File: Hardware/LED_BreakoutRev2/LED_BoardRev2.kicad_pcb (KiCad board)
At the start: 2 copper layers, 33 parts, among them Q1 BSS214NW, Q2 BSS214NW, Q3 BSS214NW, Q4 BSS214NW, Q5 BSS214NW, Q6 BSS214NW

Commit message: Concept LED layout
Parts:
- removed R13, R14: 4, MRDT_Devices:Stupid 4 Ohm Resistor
- Conn1, Q1, Q2, Q3, Q4, Q5, Q6, R2, R3: moved to B.Cu
- R1: value 250 -> 325; moved to B.Cu
- R10: value 4 -> 16; footprint MRDT_Devices:Stupid 4 Ohm Resistor -> Resistor_SMD:R_2512_6332Metric_Pad1.40x3.35mm_HandSolder; moved to B.Cu
- R11: value 4 -> 237; footprint MRDT_Devices:Stupid 4 Ohm Resistor -> Resistor_SMD:R_2512_6332Metric_Pad1.40x3.35mm_HandSolder; moved to B.Cu
- R12: value 235 -> 16; moved to B.Cu
- R4, R6, R8: value 150 -> 325; moved to B.Cu
- R5, R7: value 41 -> 39; moved to B.Cu
- R9: value 235 -> 237; moved to B.Cu
- moved Q4 167.2 mm to (55.8, 25.0), turned to 180 degrees
- moved Q2 146.0 mm to (53.5, 37.5), turned to 180 degrees
- moved Q3 139.5 mm to (71.4, 44.3), turned to 180 degrees
- moved R5 138.7 mm to (81.0, 22.1), turned to 180 degrees
- moved R4 133.2 mm to (81.0, 27.0), turned to 180 degrees
- moved R8 124.5 mm to (90.0, 22.1), turned to 180 degrees
- moved R3 121.5 mm to (102.5, 34.7), turned to 180 degrees
- moved R10 121.0 mm to (90.0, 27.0), turned to 180 degrees
- moved Q5 118.6 mm to (83.1, 41.0), turned to 180 degrees
- moved R2 115.8 mm to (102.5, 29.8), turned to 180 degrees
- moved R6 110.0 mm to (102.5, 39.6), turned to 180 degrees
- moved R11 109.9 mm to (93.4, 31.9), turned to 180 degrees
- moved R7 106.9 mm to (111.5, 34.7), turned to 180 degrees
- moved R1 106.5 mm to (111.5, 29.8), turned to 180 degrees
- moved Q6 101.4 mm to (109.4, 48.8), turned to 180 degrees
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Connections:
- R10 pad 2: Net-(R10-Pad2) -> Net-(Q5-Pad3)
- R11 pad 1: Net-(R10-Pad2) -> Net-(D11-Pad1)
- R11 pad 2: Net-(Q5-Pad3) -> Net-(Q4-Pad3)
- R12 pad 1: Net-(D11-Pad1) -> Net-(D12-Pad1)
- R12 pad 2: Net-(Q4-Pad3) -> Net-(Q5-Pad3)
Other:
- board outline added: 53.9 x 53.9 mm

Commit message: Still moving footprints
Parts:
- D5, D7: footprint MRDT_Devices:275nm LED -> Footprints:SU CULCN1.VC
- moved D7 12.3 mm to (184.7, 82.0), turned to 90 degrees
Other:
- outline, holes or cut-outs redrawn
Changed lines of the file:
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@@
   (net 23 "Net-(D9-Pad1)")
   (net 24 "Net-(D11-Pad1)")
-  (footprint "MRDT_Devices:275nm LED" (layer "F.Cu")
+  (footprint "Footprints:SU CULCN1.VC" (layer "F.Cu")
     (at 166.4016 112.3104)
     (property "Sheetfile" "LED_BoardRev2.kicad_sch")
     (property "Sheetname" "")
     (attr smd)
-    (fp_text reference "D5" (at 0.33 -2.57 unlocked) (layer "F.SilkS")
-      (effects (font (size 1 1) (thickness 0.15)))
-    )
-    (fp_text value "275nm" (at 0.33 2.91 unlocked) (layer "F.Fab")
-      (effects (font (size 1 1) (thickness 0.15)))
-    )
-    (fp_text user "${REFERENCE}" (at 0.33 4.41 unlocked) (layer "F.Fab")
-      (effects (font (size 1 1) (thickness 0.15)))
-    )
-    (fp_rect (start -1.68 1.86) (end 1.82 -1.64) (layer "F.SilkS") (width 0.12) (fill none))
-    (pad "+" smd roundrect (at 1.435 0.10775) (size 0.57 3.3155) (layers "F.Cu" "F.Paste" "F.Mask") (roundrect_rratio 0.1))
-    (pad "-" smd roundrect (at -1.295 0.11) (size 0.57 3.32) (layers "F.Cu" "F.Paste" "F.Mask") (roundrect_rratio 0.1))
-    (pad "ESD" smd roundrect (at 0.07 0.11) (size 1.32 3.32) (layers "F.Cu" "F.Paste" "F.Mask") (roundrect_rratio 0.1))
+    (fp_text reference "D5" (at 0 -4 unlocked) (layer "F.SilkS")
+      (effects (font (size 1 1) (thickness 0.15)))
+    )
+    (fp_text value "275nm" (at 0 4.1 unlocked) (layer "F.Fab")
+      (effects (font (size 1 1) (thickness 0.15)))
+    )
+    (fp_text user "${REFERENCE}" (at 0 6 unlocked) (layer "F.Fab")
+      (effects (font (size 1 1) (thickness 0.15)))
+    )
+    (fp_line (start -2.8 -3.1) (end 2.8 -3.1) (layer "F.SilkS") (width 0.12))
+    (fp_line (start 2.8 3.1) (end -2.8 3.1) (layer "F.SilkS") (width 0.12))
+    (fp_line (start 2.8 -3.1) (end 2.8 3.1) (layer "F.SilkS") (width 0.12))
+    (fp_line (start -2.8 3.1) (end -2.8 -3.1) (layer "F.SilkS") (width 0.12))
+    (pad "1" smd rect (at -1.925 0) (size 1.55 3.4) (layers "F.Cu" "F.Paste" "F.Mask")
+      (net 21 "Net-(D5-Pad1)") (pinfunction "K") (pintype "passive"))
+    (pad "2" smd rect (at 1.925 0) (size 1.55 3.4) (layers "F.Cu" "F.Paste" "F.Mask")
+      (net 1 "+12V") (pinfunction "A") (pintype "passive"))
+    (pad "3" smd custom (at 0 0) (size 1 4) (layers "F.Cu" "F.Paste" "F.Mask")
+      (options (clearance outline) (anchor rect))
+      (primitives
+        (gr_rect (start 2.7 -3.02) (end -2.7 -2) (width 0.01) (fill yes))
+        (gr_rect (start 2.7 2) (end -2.7 3.02) (width 0.01) (fill yes))
+      ))
   )
   (footprint "MRDT_Devices:310nm" (layer "F.Cu")
@@
     )
     (fp_rect (start -1.725 -1.775) (end 1.725 1.675) (layer "F.SilkS") (width 0.12) (fill none))
-    (fp_arc (start 0.01 -0.19) (mid 0.190064 0.00487) (end 0 0.19) (layer "F.SilkS") (width 0.12))
+    (fp_arc (start 0.01 -0.19) (mid 0.190063 0.00487) (end 0 0.19) (layer "F.SilkS") (width 0.12))
     (fp_rect (start 0.25 -1.625) (end 1.575 1.525) (layer "Dwgs.User") (width 0.12) (fill none))
     (fp_rect (start -1.575 0.25) (end -2.025 -0.25) (layer "Dwgs.User") (width 0.12) (fill none))
@@
     )
     (fp_rect (start -1.725 -1.775) (end 1.725 1.675) (layer "F.SilkS") (width 0.12) (fill none))
-    (fp_arc (start 0.01 -0.19) (mid 0.190064 0.00487) (end 0 0.19) (layer "F.SilkS") (width 0.12))
+    (fp_arc (start 0.01 -0.19) (mid 0.190063 0.00487) (end 0 0.19) (layer "F.SilkS") (width 0.12))
     (fp_rect (start 2.025 0.25) (end 1.575 -0.25) (layer "Dwgs.User") (width 0.12) (fill none))
     (fp_rect (start 0.25 -1.625) (end 1.575 1.525) (layer "Dwgs.User") (width 0.12) (fill none))
@@
     (pad "3" smd roundrect (at 1.8 0) (size 0.57 0.62) (layers "F.Cu" "F.Paste" "F.Mask") (roundrect_rratio 0.1))
   )
-  (footprint "MRDT_Devices:275nm LED" (layer "F.Cu")
-    (at 184.8674 69.7654)
-    (property "Sheetfile" "LED_BoardRev2.kicad_sch")
-    (property "Sheetname" "")
-    (attr smd)
-    (fp_text reference "D7" (at 0.33 -2.57 unlocked) (layer "F.SilkS")
-      (effects (font (size 1 1) (thickness 0.15)))
-    )
-    (fp_text value "275nm" (at 0.33 2.91 unlocked) (layer "F.Fab")
-      (effects (font (size 1 1) (thickness 0.15)))
-    )
-    (fp_text user "${REFERENCE}" (at 0.33 4.41 unlocked) (layer "F.Fab")
-      (effects (font (size 1 1) (thickness 0.15)))
-    )
-    (fp_rect (start -1.68 1.86) (end 1.82 -1.64) (layer "F.SilkS") (width 0.12) (fill none))
-    (pad "+" smd roundrect (at 1.435 0.10775) (size 0.57 3.3155) (layers "F.Cu" "F.Paste" "F.Mask") (roundrect_rratio 0.1))
-    (pad "-" smd roundrect (at -1.295 0.11) (size 0.57 3.32) (layers "F.Cu" "F.Paste" "F.Mask") (roundrect_rratio 0.1))
-    (pad "ESD" smd roundrect (at 0.07 0.11) (size 1.32 3.32) (layers "F.Cu" "F.Paste" "F.Mask") (roundrect_rratio 0.1))
+  (footprint "Footprints:SU CULCN1.VC" (layer "F.Cu")
+    (at 184.6834 82.0166 90)
+    (property "Sheetfile" "LED_BoardRev2.kicad_sch")
+    (property "Sheetname" "")
+    (attr smd)
+    (fp_text reference "D7" (at 0 -4 90 unlocked) (layer "F.SilkS")
+      (effects (font (size 1 1) (thickness 0.15)))
+    )
+    (fp_text value "275nm" (at 0 4.1 90 unlocked) (layer "F.Fab")
+      (effects (font (size 1 1) (thickness 0.15)))
+    )
+    (fp_text user "${REFERENCE}" (at 0 6 90 unlocked) (layer "F.Fab")
+      (effects (font (size 1 1) (thickness 0.15)))
+    )
+    (fp_line (start -2.8 -3.1) (end 2.8 -3.1) (layer "F.SilkS") (width 0.12))
+    (fp_line (start 2.8 3.1) (end -2.8 3.1) (layer "F.SilkS") (width 0.12))
+    (fp_line (start -2.8 3.1) (end -2.8 -3.1) (layer "F.SilkS") (width 0.12))
+    (fp_line (start 2.8 -3.1) (end 2.8 3.1) (layer "F.SilkS") (width 0.12))
+    (pad "1" smd rect (at -1.925 0 90) (size 1.55 3.4) (layers "F.Cu" "F.Paste" "F.Mask")
+      (net 22 "Net-(D7-Pad1)") (pinfunction "K") (pintype "passive"))
+    (pad "2" smd rect (at 1.925 0 90) (size 1.55 3.4) (layers "F.Cu" "F.Paste" "F.Mask")
+      (net 1 "+12V") (pinfunction "A") (pintype "passive"))
+    (pad "3" smd custom (at 0 0 90) (size 1 4) (layers "F.Cu" "F.Paste" "F.Mask")
+      (options (clearance outline) (anchor rect))
+      (primitives
+        (gr_rect (start 2.7 -3.02) (end -2.7 -2) (width 0.01) (fill yes))
+        (gr_rect (start 2.7 2) (end -2.7 3.02) (width 0.01) (fill yes))
+      ))
   )
   (footprint "Resistor_SMD:R_2512_6332Metric_Pad1.40x3.35mm_HandSolder" (layer "B.Cu")
@@
   (gr_rect (start 156.6672 71.9328) (end 194.7672 110.0328) (layer "Dwgs.User") (width 0.15) (fill none))
   (gr_line (start 156.6672 90.9828) (end 175.7172 90.9828) (layer "Dwgs.User") (width 0.15))
+  (gr_rect (start 166.751 99.949) (end 175.7172 90.9828) (layer "Edge.Cuts") (width 0.1) (fill none))
   (gr_circle (center 175.7172 90.9828) (end 178.2572 90.9828) (layer "Edge.Cuts") (width 0.1) (fill none))
   (gr_line (start 175.7172 90.9828) (end 178.2572 90.9828) (layer "Edge.Cuts") (width 0.1))
   (gr_circle (center 175.7172 90.9828) (end 175.7172 78.2828) (layer "Edge.Cuts") (width 0.1) (fill none))
   (gr_circle (center 175.7172 90.9828) (end 202.657968 90.9828) (layer "Edge.Cuts") (width 0.15) (fill none))
+  (gr_rect (start 175.7172 90.9828) (end 184.6834 82.0166) (layer "Edge.Cuts") (width 0.1) (fill none))
 )

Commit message: Changing layout
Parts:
- D10, D12: footprint MRDT_Devices:365nm LED -> Footprints:LZ1-00UV0R
- moved D2 61.1 mm to (142.2, 114.3), turned to 45 degrees
- moved De 55.9 mm to (142.2, 104.1), turned to -45 degrees
- moved D1 51.2 mm to (145.2, 100.4)
- moved D8 46.2 mm to (145.7, 117.2), turned to -135 degrees
- moved D5 44.8 mm to (121.7, 109.2)
- moved D10 43.8 mm to (137.2, 124.5)
- moved D7 42.0 mm to (152.7, 109.2), turned to 0 degrees
- moved D12 41.6 mm to (137.2, 94.0)
- moved Conn1 40.1 mm to (167.4, 22.1)
- moved D11 38.1 mm to (132.1, 114.3), turned to -45 degrees
- moved D6 38.0 mm to (128.3, 101.2)
- moved D4 30.6 mm to (129.1, 118.0), turned to 135 degrees
- moved D3 24.5 mm to (132.1, 104.1), turned to 45 degrees
- renumbered D9 to De
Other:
- board size 53.9 x 53.9 mm -> 43.2 x 43.2 mm

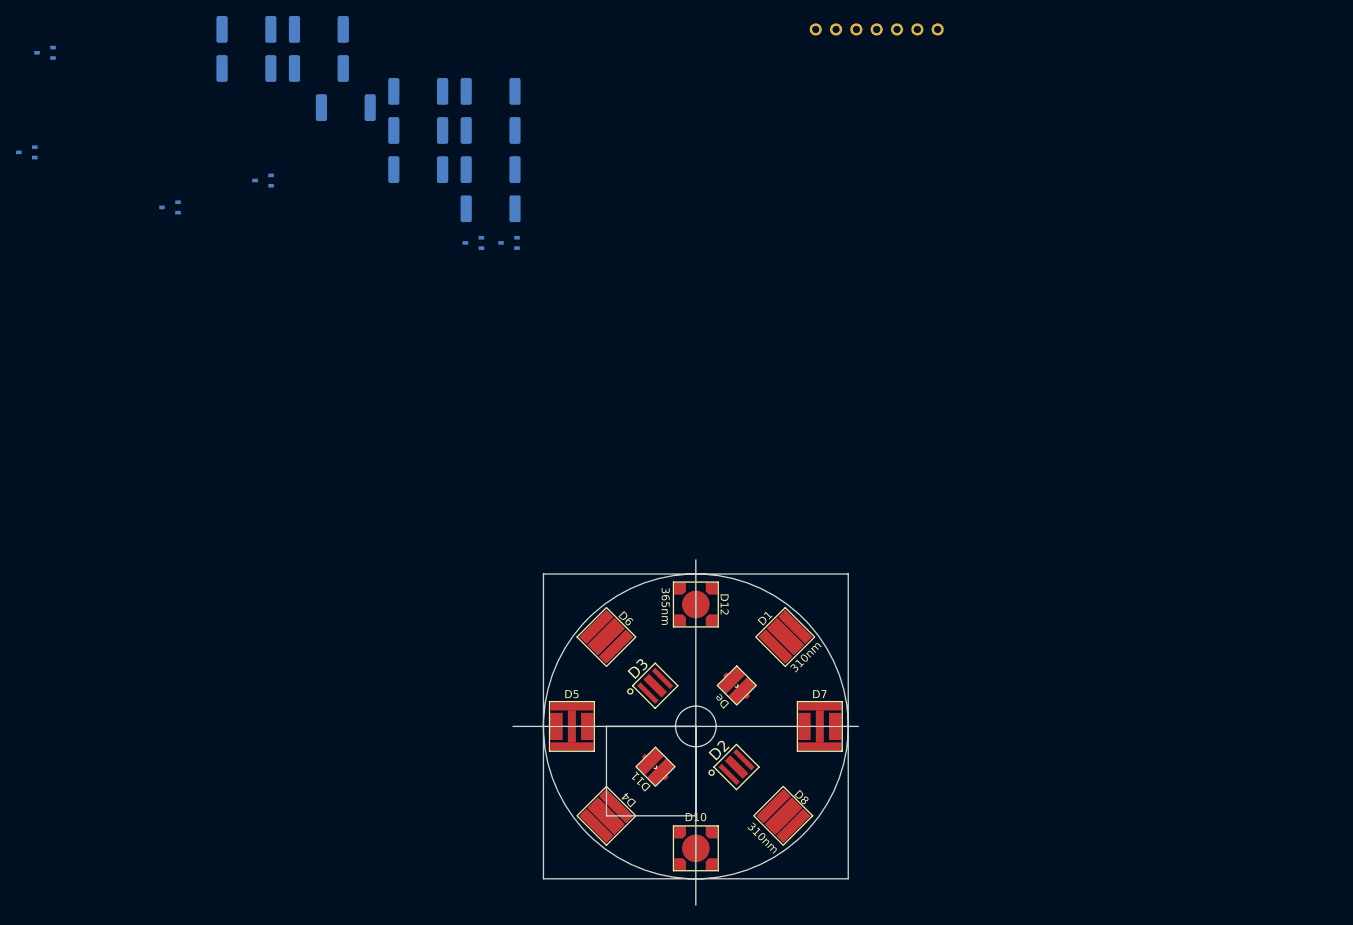
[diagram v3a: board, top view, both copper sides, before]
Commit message: Moving MOSFTETs over to instruments board
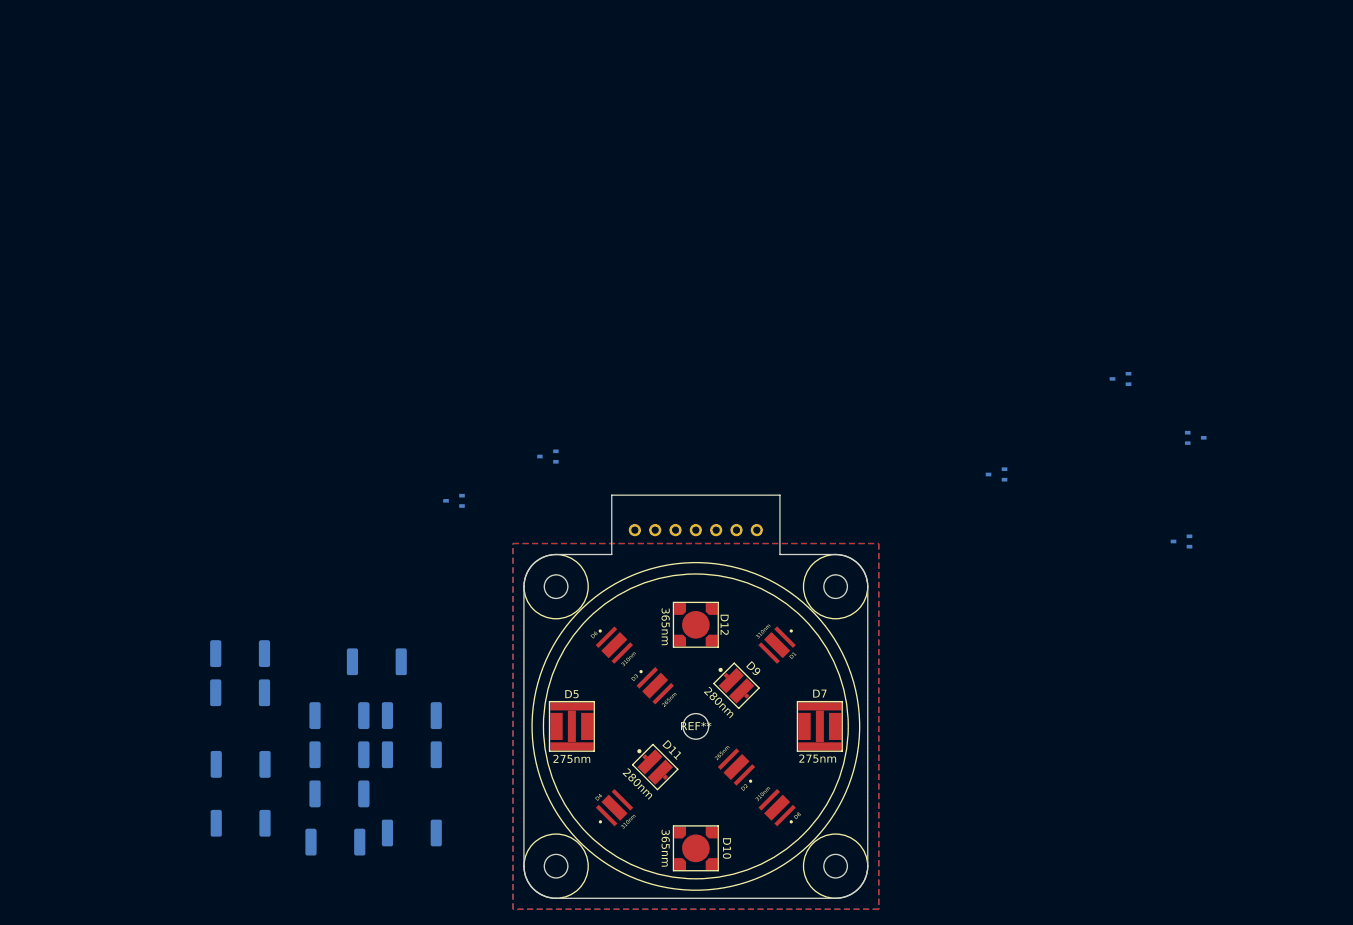
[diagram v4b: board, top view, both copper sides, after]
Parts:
- added H1: MountingHole, MRDT_Drill_Holes:4_40_Hole_Corner, F.Cu at (150.6, 95.8)
- added H2: MountingHole, MRDT_Drill_Holes:4_40_Hole_Corner, F.Cu at (150.6, 122.7)
- added H3: MountingHole, MRDT_Drill_Holes:4_40_Hole_Corner, F.Cu at (123.7, 122.7)
- added H4: MountingHole, MRDT_Drill_Holes:4_40_Hole_Corner, F.Cu at (123.7, 95.8)
- added REF**: MountingHole_3.2mm_M3, MountingHole:MountingHole_3.2mm_M3, F.Cu at (137.2, 109.2)
- D1, D4, D6, D8: footprint MRDT_Devices:310nm -> Footprints:1414_3535_Metric
- D11: footprint MRDT_Devices:280nm -> Footprints:VLMU35CL2.-275-120
- D2, D3: footprint KL265-50W-SM-WD Footprint:3535 -> Footprints:1414_3535_Metric
- D9: renamed from De; footprint MRDT_Devices:280nm -> Footprints:VLMU35CL2.-275-120
- moved Q3 131.4 mm to (199.6, 73.2), turned to 0 degrees
- moved Q2 127.7 mm to (174.8, 77.7)
- moved Q5 123.4 mm to (197.9, 86.1)
- moved R5 102.2 mm to (92.1, 123.7), turned to 0 degrees
- moved R4 94.4 mm to (80.3, 121.3), turned to 0 degrees
- moved R11 83.1 mm to (80.3, 114.0), turned to 0 degrees
- moved Q6 82.7 mm to (190.2, 65.8)
- moved R1 78.6 mm to (101.7, 107.9)
- moved R10 78.6 mm to (80.2, 105.0)
- moved R12 78.6 mm to (101.7, 122.5)
- moved R2 78.6 mm to (92.6, 107.9)
- moved R3 78.6 mm to (92.6, 112.8)
- moved R6 78.6 mm to (92.6, 117.7)
- moved R7 78.6 mm to (101.7, 112.8)
- moved R8 78.6 mm to (80.2, 100.1)
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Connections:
- Q6 pad 3: Net-(Q5-Pad3) -> Net-(Q6-Pad3)
- R12 pad 2: Net-(Q5-Pad3) -> Net-(Q6-Pad3)
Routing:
- added copper zone on B.Cu, net GND
- added copper zone on F.Cu, net GND
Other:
- board size 43.2 x 43.2 mm -> 43 x 50.4 mm

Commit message: Finished LED Board Rev2
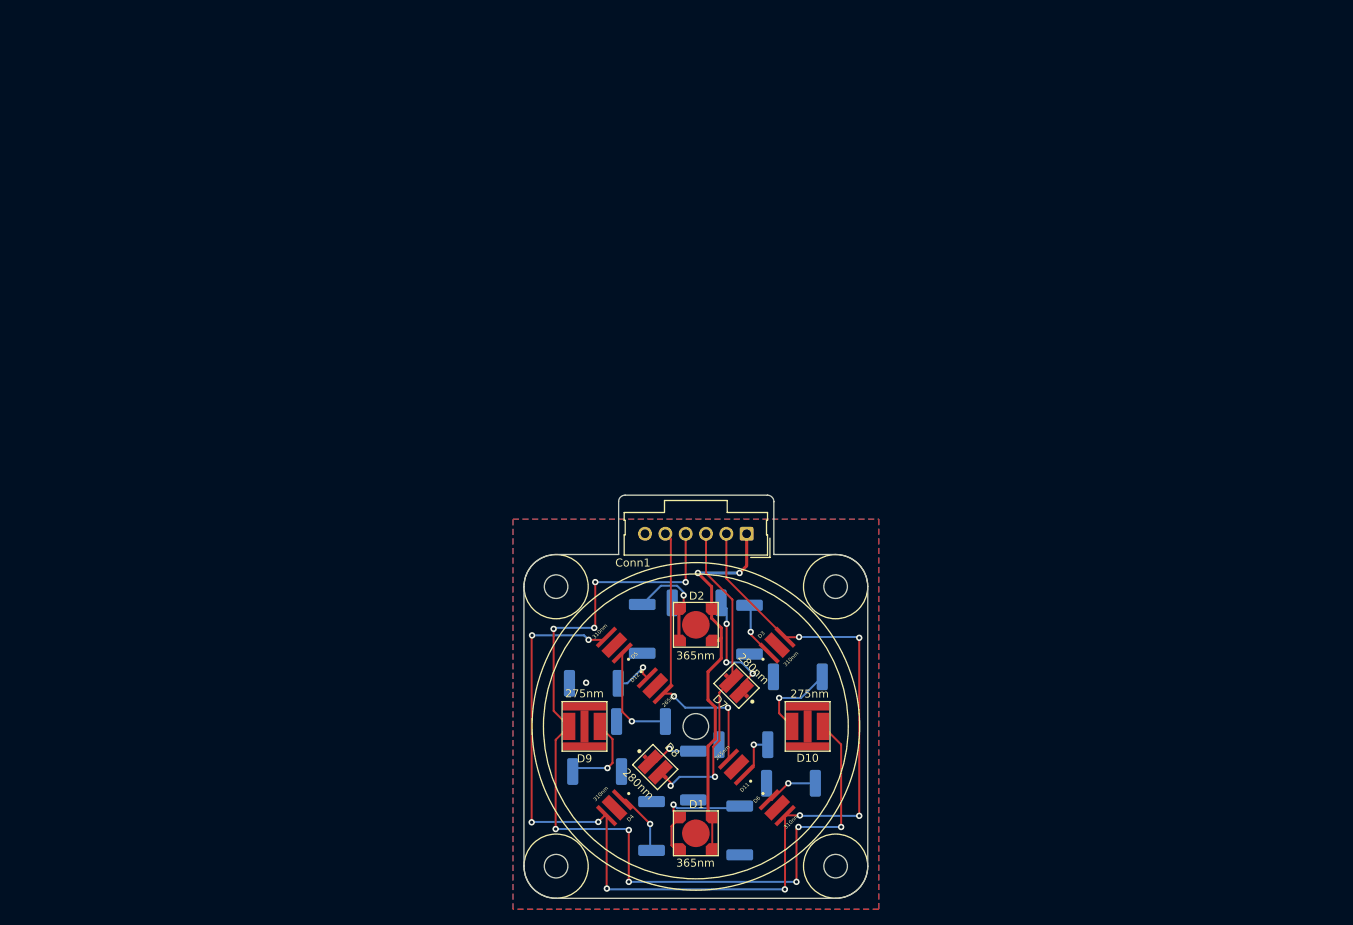
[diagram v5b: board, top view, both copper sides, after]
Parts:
- removed Q1, Q2, Q3, Q4, Q5, Q6: BSS214NW, Package_TO_SOT_SMD:SOT-323_SC-70
- Conn1: value Molex_SL_07 -> Molex_uF_D_06; footprint MRDT_Connectors:MOLEX_SL_07_Vertical -> Connector_Molex:Molex_SL_171971-0006_1x06_P2.54mm_Vertical; moved to F.Cu
- moved R6 70.7 mm to (149.0, 116.3)
- moved R1 64.8 mm to (142.6, 122.2), turned to -90 degrees
- moved R8 56.6 mm to (136.9, 115.4), turned to -90 degrees
- moved R4 51.4 mm to (131.6, 121.7), turned to 90 degrees
- moved R11 50.6 mm to (143.1, 111.5)
- moved R10 49.2 mm to (149.9, 103.0)
- moved R3 43.6 mm to (143.9, 97.1), turned to -90 degrees
- moved R7 40.7 mm to (137.3, 93.8)
- moved R5 38.8 mm to (130.3, 108.6)
- moved R2 38.5 mm to (130.5, 97.0), turned to -90 degrees
- moved R9 33.9 mm to (124.8, 114.9)
- moved R12 33.0 mm to (124.4, 103.8)
- moved D1 1.88 mm to (137.2, 122.6)
- moved D9 1.57 mm to (123.2, 109.2), turned to 180 degrees
- moved D10 1.52 mm to (151.1, 109.2), turned to 0 degrees
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- renumbered D10 to D1, D7 to D10, D2 to D11, D3 to D12, D12 to D2, D1 to D3, D6 to D5, D8 to D6, D9 to D7, D11 to D8, D5 to D9, R10 to R1, R7 to R10, R2 to R11, R3 to R12, R12 to R2, R1 to R3, R6 to R5, R8 to R6, R9 to R7, R11 to R8, R5 to R9
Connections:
- Conn1 pad 1: +12V -> /365nm
- Conn1 pad 2: /365nm -> /310nm
- Conn1 pad 3: /310nm -> /280nm
- Conn1 pad 4: /280nm -> /275nm
- Conn1 pad 5: /275nm -> /260nm
- Conn1 pad 6: /260nm -> GND
- D1 pad 2: +12V -> /365nm
- D10 pad 2: +12V -> /275nm
- D11 pad 2: +12V -> /260nm
- D12 pad 2: +12V -> /260nm
- D2 pad 2: +12V -> /365nm
- D3 pad 2: +12V -> /310nm
- D4 pad 2: +12V -> /310nm
- D5 pad 2: +12V -> /310nm
- D6 pad 2: +12V -> /310nm
- D7 pad 2: +12V -> /280nm
- D8 pad 2: +12V -> /280nm
- D9 pad 2: +12V -> /275nm
- R1 pad 2: Net-(Q5-Pad3) -> GND
- R10 pad 2: Net-(Q3-Pad3) -> GND
- R11 pad 2: Net-(Q1-Pad3) -> GND
- R12 pad 2: Net-(Q1-Pad3) -> GND
- R2 pad 2: Net-(Q6-Pad3) -> GND
- R3 pad 2: Net-(Q2-Pad3) -> GND
- R4 pad 2: Net-(Q2-Pad3) -> GND
- R5 pad 2: Net-(Q2-Pad3) -> GND
- R6 pad 2: Net-(Q2-Pad3) -> GND
- R7 pad 2: Net-(Q4-Pad3) -> GND
- R8 pad 2: Net-(Q4-Pad3) -> GND
- R9 pad 2: Net-(Q3-Pad3) -> GND
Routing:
- net /310nm: track 0.00 -> 140.3 mm, vias 0 -> 10
- net /275nm: track 0.00 -> 117.2 mm, vias 0 -> 10
- net /365nm: track 0.00 -> 49.7 mm, vias 0 -> 2
- net /280nm: track 0.00 -> 41.0 mm, vias 0 -> 2
- net /260nm: track 0.00 -> 36.0 mm, vias 0 -> 2
- net Net-(D1-Pad1): track 0.00 -> 15.7 mm, vias 0 -> 1
- net Net-(D7-Pad1): track 0.00 -> 14.4 mm, vias 0 -> 3
- net Net-(D5-Pad1): track 0.00 -> 13.2 mm, vias 0 -> 1
- net Net-(D2-Pad1): track 0.00 -> 12.8 mm, vias 0 -> 1
- net Net-(D10-Pad1): track 0.00 -> 10.7 mm, vias 0 -> 1
- net Net-(D9-Pad1): track 0.00 -> 10.6 mm, vias 0 -> 1
- net Net-(D4-Pad1): track 0.00 -> 8.08 mm, vias 0 -> 1
- net Net-(D3-Pad1): track 0.00 -> 6.99 mm, vias 0 -> 1
- net Net-(D6-Pad1): track 0.00 -> 6.62 mm, vias 0 -> 1
- net Net-(D8-Pad1): track 0.00 -> 6.23 mm, vias 0 -> 1
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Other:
- outline, holes or cut-outs redrawn
